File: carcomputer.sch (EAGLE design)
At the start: 39 parts, among them K1 351, Q1 BUZ10, Q2 BUZ10, T1 2N2219

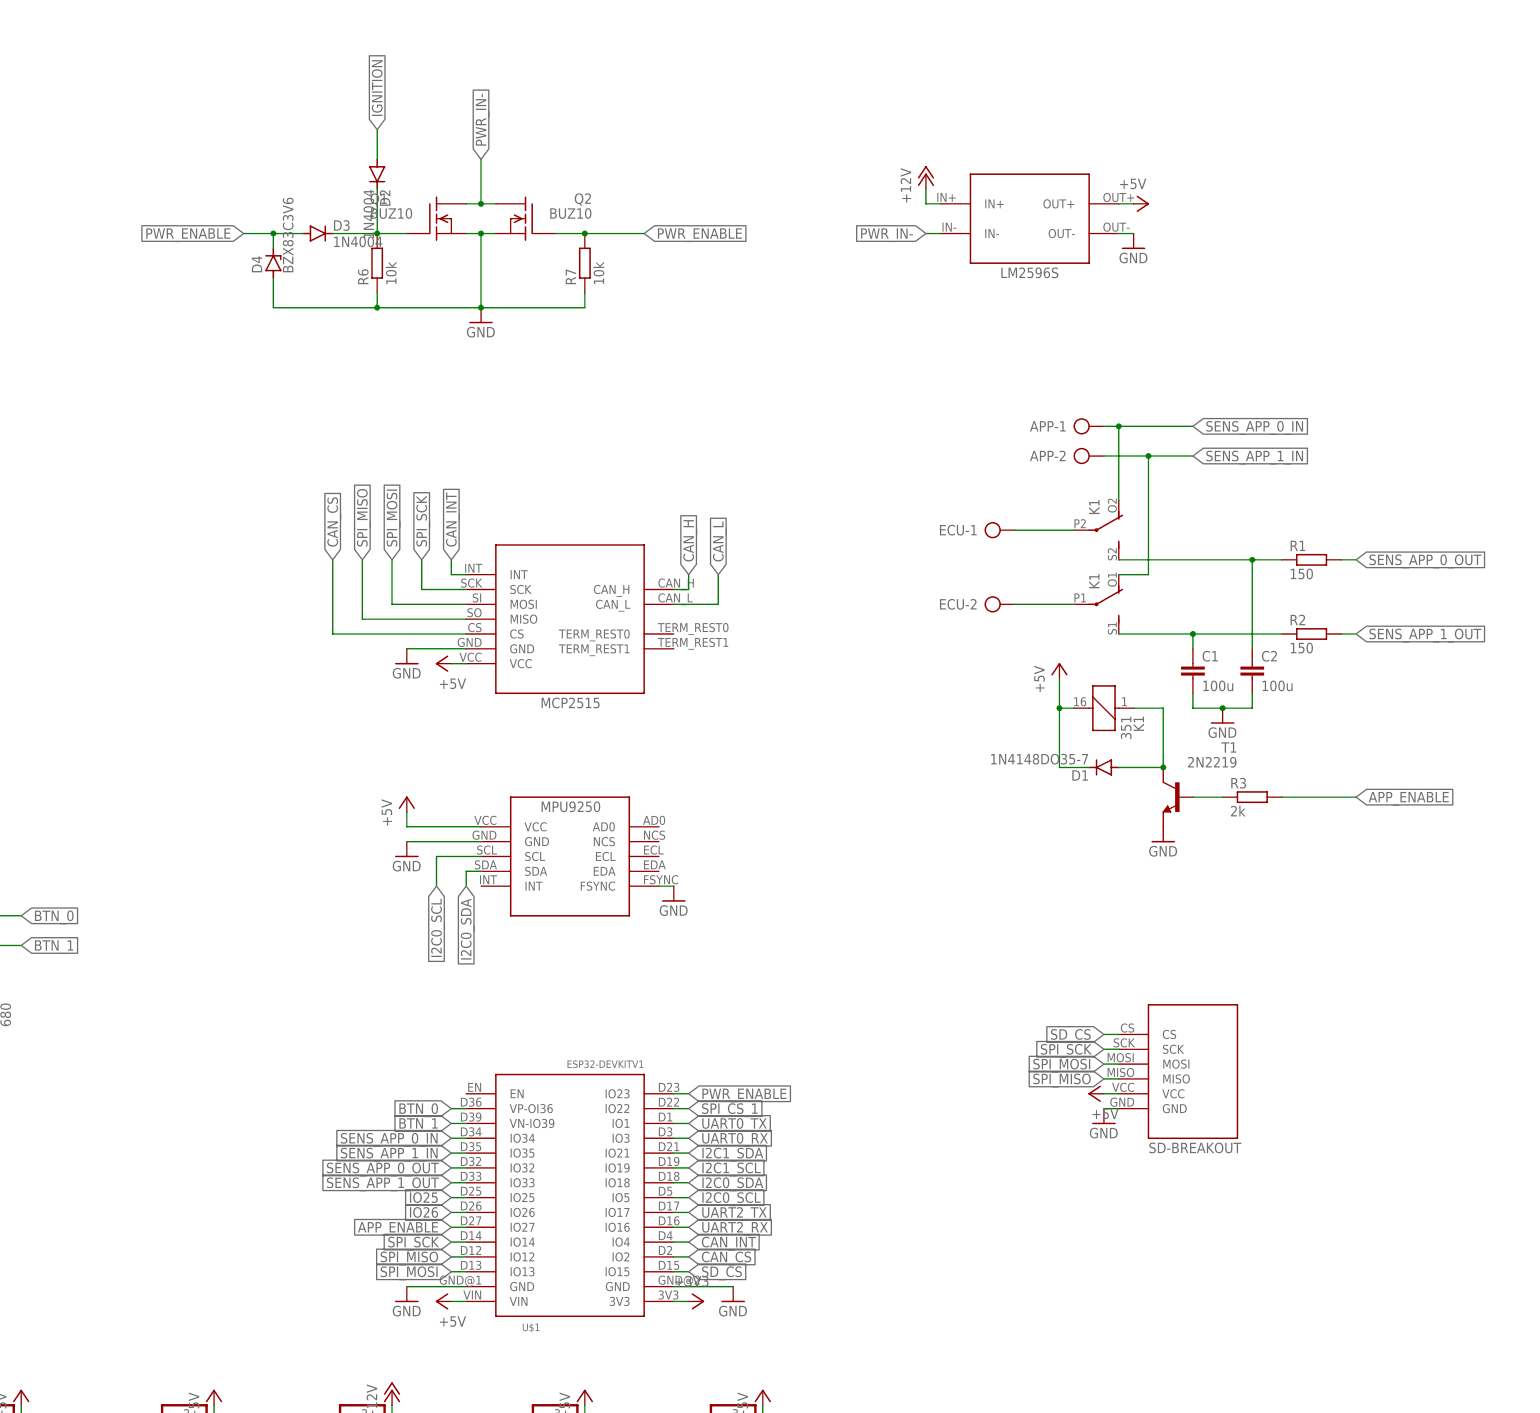
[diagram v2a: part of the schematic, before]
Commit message: Added voltage divider to input APP"
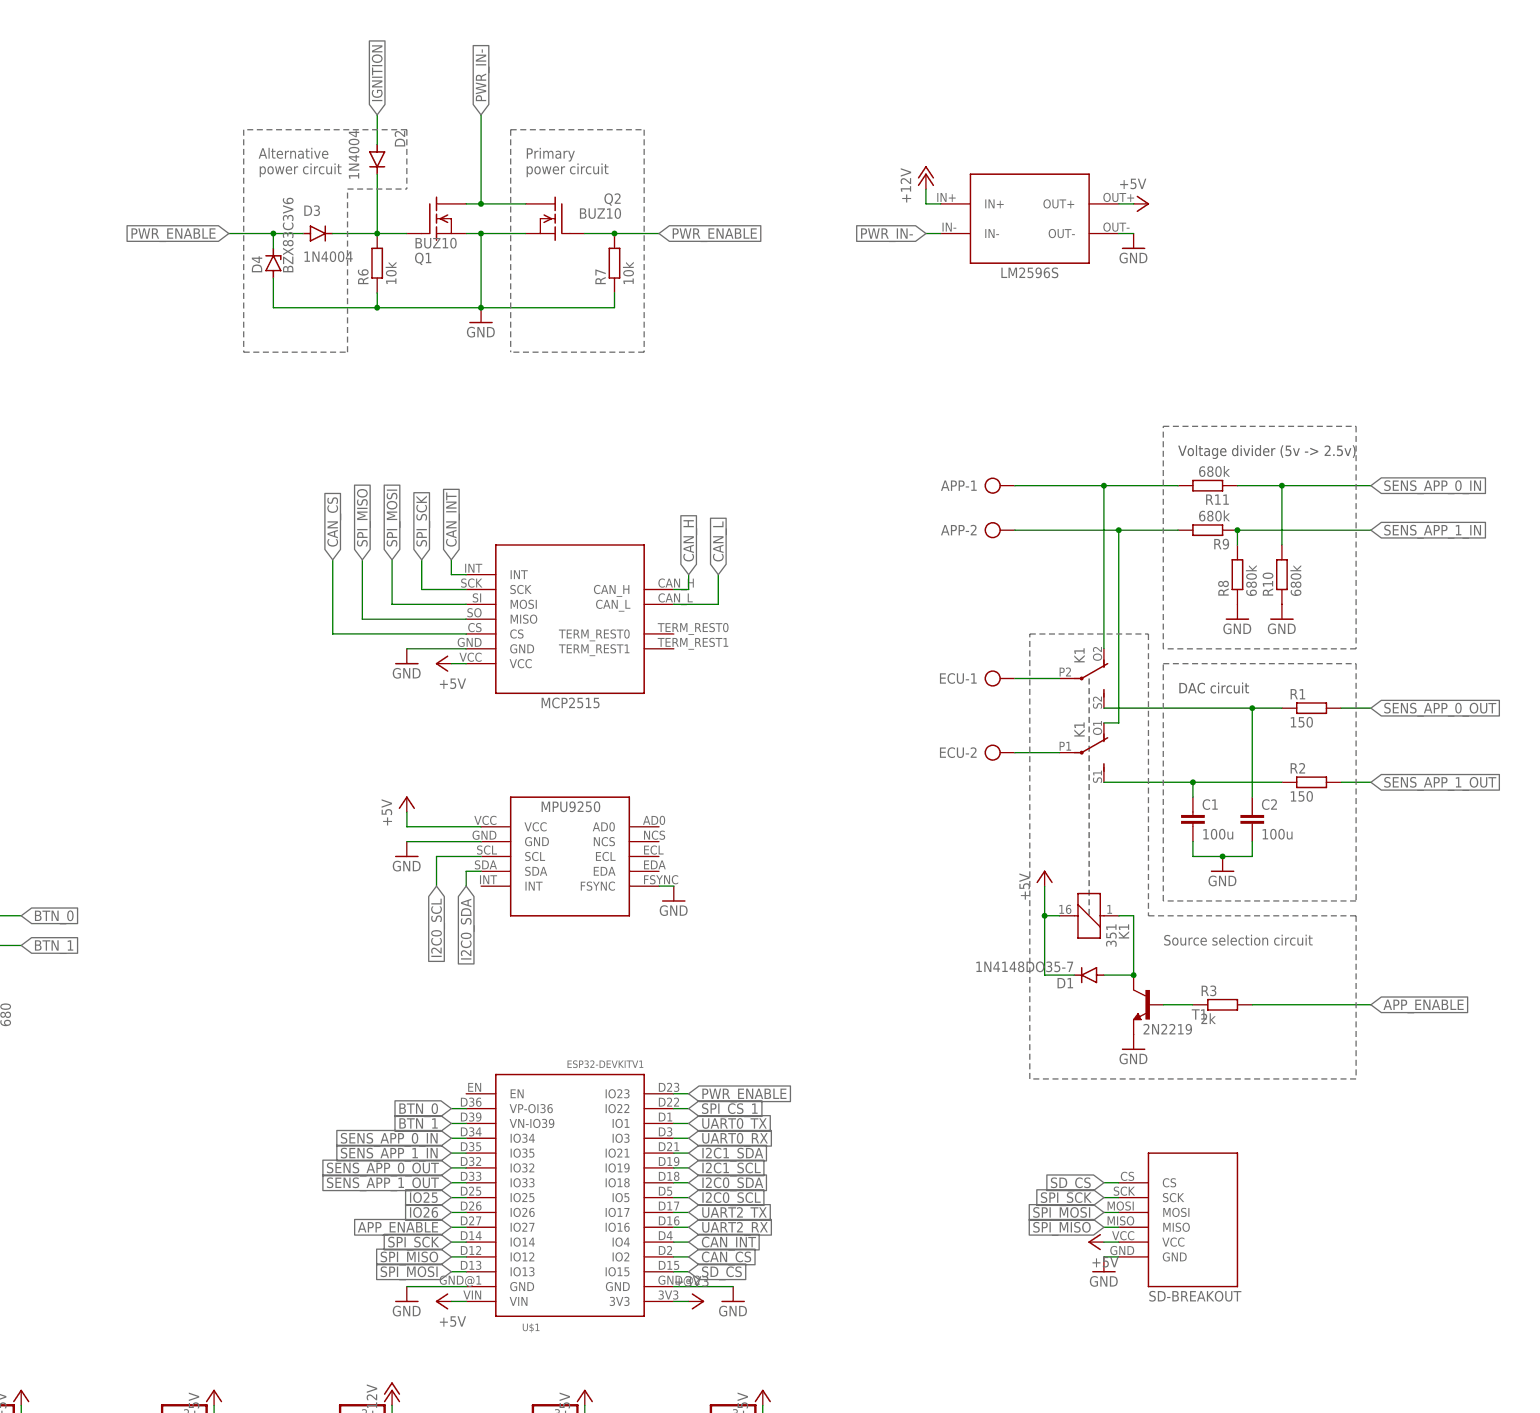
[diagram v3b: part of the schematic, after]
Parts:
- added R10, R11, R8, R9: 680k, rcl:R-EU_0207/7
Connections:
- new net APP_0_IN: APP-1.KL, K13.O, R11.2
- new net APP_1_IN: APP-2.KL, K12.O, R9.2
- net GND: now also R10.1, R8.1
- net SENS_APP_0_IN: now also R10.2, R11.1; no longer APP-1.KL, K13.O
- net SENS_APP_1_IN: now also R8.2, R9.1; no longer APP-2.KL, K12.O
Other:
- note added: "Alternative power circuit"
- note added: "DAC circuit"
- note added: "Primary power circuit"
- note added: "Source selection circuit"
- note added: "Voltage divider (5v -> 2.5v)"
- moved on the sheet: APP-1, APP-2, C1, C2, D1, D2, ECU-1, ECU-2, K1, Q2, R1, R2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

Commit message: Added A9G GPS unit. Removed backup files from git
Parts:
- added Q3, Q4: TIP136, transistor-pnp:TIP136
- added R12, R13, R14: 2k, rcl:R-EU_0207/7
- added R15: 5k, rcl:R-EU_0207/7
- added S1: (no value), switch-omron:10-XX
- added U$6: A9G, A9:A9G
- added U$7: BI-DIRECTIONAL1, level-converter:BI-DIRECTIONAL1
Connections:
- removed net SENS_APP_0_OUT: R1.2, U$1.IO32
- removed net SENS_APP_1_OUT: R2.2, U$1.IO33
- new net APP_PWM_OUT_0: R13.2, U$1.IO32
- new net APP_PWM_OUT_1: R12.2, U$1.IO33
- new net GPS_RX: U$6.IO0/RX1, U$7.RX_H1
- new net GPS_TX: U$6.IO1/TX1, U$7.TX_H1
- new net MCU_RESET: S1.P, S1.P1, U$1.EN, U$6.RST
- new net N$10: R14.1, U$2.INT
- new net N$11: Q4.C, R1.2
- new net N$13: Q4.B, R13.1
- new net N$8: Q3.B, R12.1
- new net N$9: Q3.C, R2.2
- net +3V3: now also DISPLAY-4.1, U$3.VCC, U$7.LV
- net +5V: now also Q3.E, Q4.E, U$6.5V, U$7.HV; no longer DISPLAY-4.1, U$3.VCC
- net CAN_INT: now also R14.2, R15.2; no longer U$2.INT
- net GND: now also R15.1, S1.S, S1.S1, U$6.GND, U$6.GND2, U$7.GND
- net SPI_MISO: now also U$1.IO13; no longer U$1.IO12
- net SPI_MOSI: now also U$1.IO12; no longer U$1.IO13
- net UART2_RX: now also U$7.RX_L1
- net UART2_TX: now also U$7.TX_L1
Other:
- moved on the sheet: APP-1, APP-2, C1, C2, D1, ECU-1, ECU-2, K1, R1, R10, R11, R2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

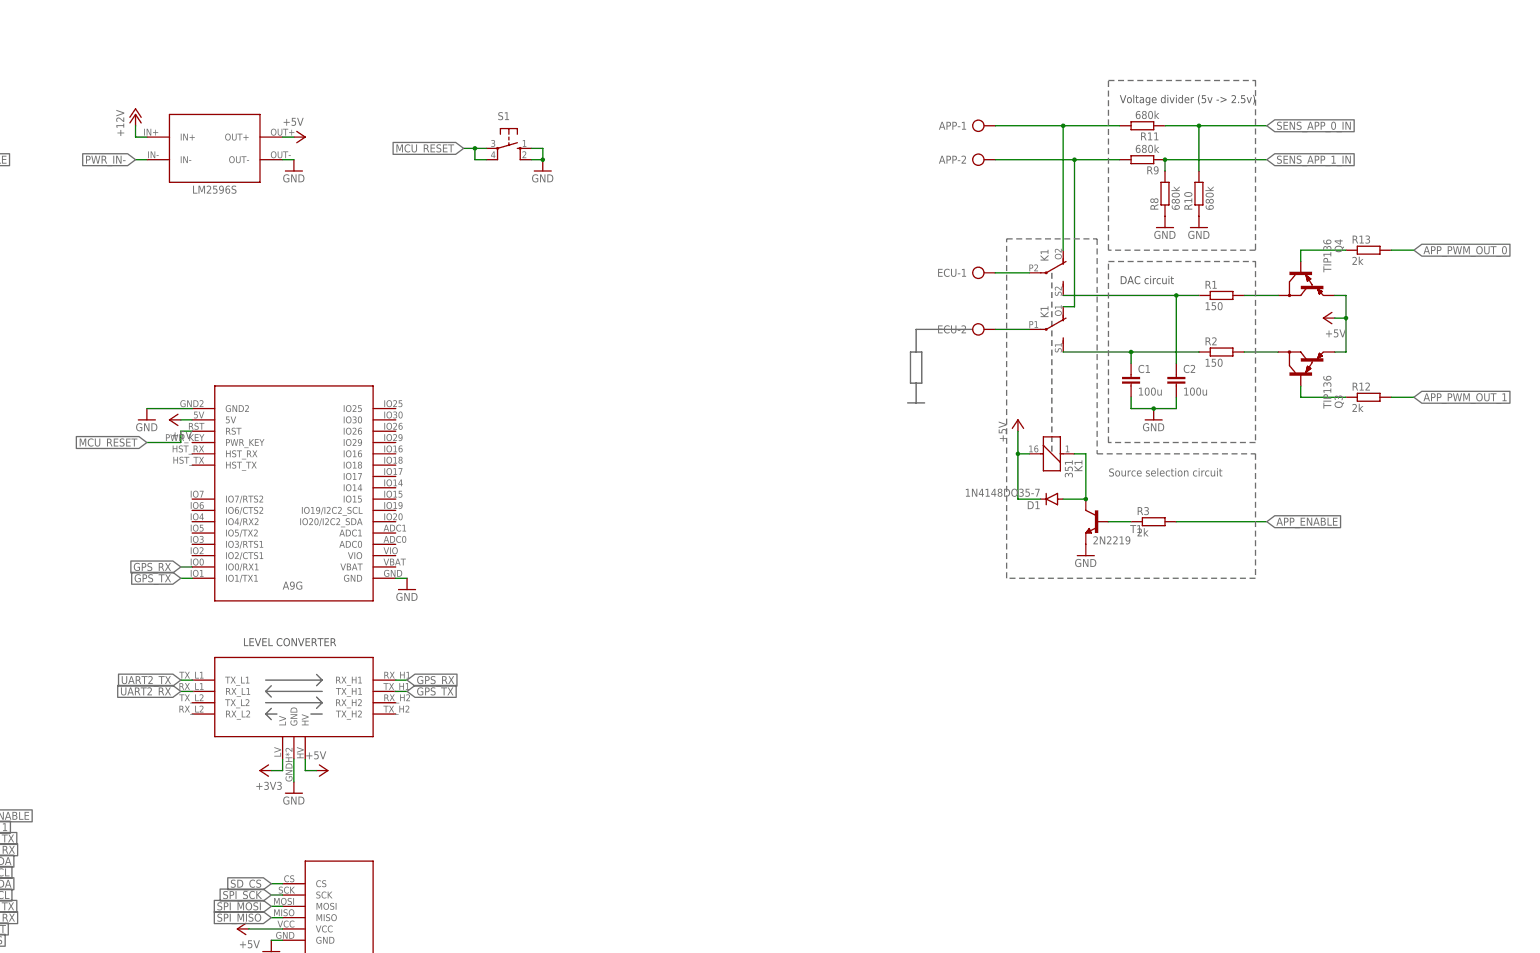
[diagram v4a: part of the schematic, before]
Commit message: Changed GPS level converter to external resistor using level converter internal resistor
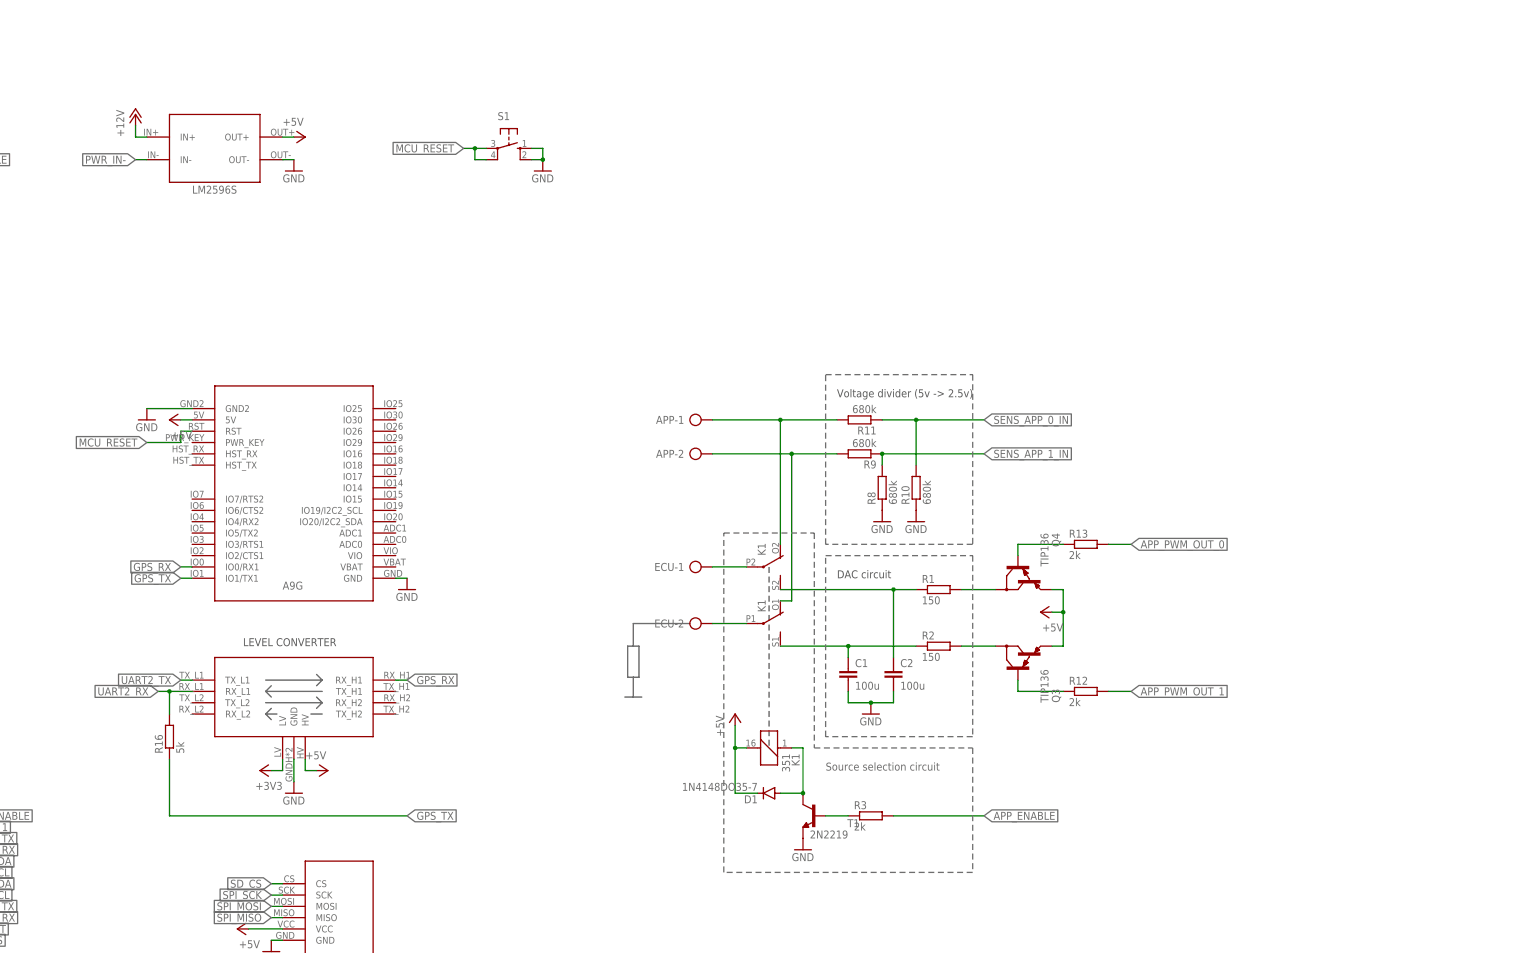
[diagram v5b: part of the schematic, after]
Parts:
- added R16: 5k, rcl:R-EU_0207/7
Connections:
- net GPS_TX: now also R16.1; no longer U$7.TX_H1
- net UART2_RX: now also R16.2
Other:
- moved on the sheet: APP-1, APP-2, C1, C2, D1, ECU-1, ECU-2, K1, Q3, Q4, R1, R10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

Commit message: Fixed power circuit
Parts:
- removed Q1, Q2: BUZ10, transistor-fet:BUZ10
- removed R7: 10k, rcl:R-EU_0207/7
- added Q5: TIP136, transistor-pnp:TIP136
- added R17: 26k, rcl:R-EU_0207/7
- added R18, R19: 10k, rcl:R-EU_0207/7
- added T2: 2N2219, transistor:2N2219
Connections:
- removed net PWR_IN-: Q1.D, Q2.D, U$4.IN-
- new net N$12: D2.A, R17.1
- new net N$14: Q5.B, R18.1
- new net N$15: R18.2, R19.1, T2.C
- new net PWR_IN+: Q5.C, U$4.IN+
- net +12V: now also Q5.E, R19.2; no longer U$4.IN+
- net GND: now also T2.E, U$4.IN-; no longer Q1.S, Q2.S, R7.1
- net IGNITION: now also R17.2; no longer D2.A
- net N$5: now also T2.B; no longer Q1.G
- net PWR_ENABLE: no longer Q2.G, R7.2
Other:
- note added: "?"
- note added: "ACCELERATOR PEDAL SWITCH/DAC"
- note added: "AUTO POWER MANAGEMENT"
- note added: "EXTRA CONNECTORS"
- note added: "Over voltage protection"
- note removed: "Alternative power circuit"
- note removed: "Primary power circuit"
- moved on the sheet: D2, D3, D4, JP_I2C_1, JP_I2C_2, JP_IO25, JP_IO26, JP_PWR_12V, JP_PWR_3V3, JP_PWR_5V_1, JP_PWR_5V_2, JP_SPI_1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

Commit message: Fixed 3V->5V gas pedal converter at high frequencies with opamp after DAC
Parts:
- removed Q3, Q4: TIP136, transistor-pnp:TIP136
- added C3: 100u, rcl:C-EU025-050X050
- added D5, D6: BZX83C5V6, diode:BZX85
- added D7, D8: 1N4148DO35-7, diode:1N4148DO35-7
- added IC1: LM358N, linear:LM358N
- added Q6: BUZ72, transistor-fet:BUZ72
- added Q7: BUZ171, transistor-fet:BUZ171
- added R20, R28, R7: 2k, rcl:R-EU_0207/7
- added R21, R26: 1k, rcl:R-EU_0207/7
- added R24: 150, rcl:R-EU_0207/7
- added R25: 500?, rcl:R-EU_0207/7
- added R27: 10k, rcl:R-EU_0207/7
- R12, R13: value 2k -> 1k
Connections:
- new net IN: Q6.G, R28.2
- new net N$16: IC1B.-IN, R13.2, R20.1
- new net N$21: C3.1, R24.2, R25.2
- new net N$24: Q7.G, R26.2, R27.1
- new net OUT: Q7.D, R24.1
- net +12V: now also IC1P.V+
- net +5V: now also D7.C, D8.C, Q7.S, R27.2; no longer Q3.E, Q4.E
- net APP_PWM_OUT_0: now also R1.2; no longer R13.2
- net APP_PWM_OUT_1: now also R2.2; no longer R12.2
- net GND: now also C3.2, D5.A, D6.A, IC1P.V-, Q6.D, Q6.S, R20.2, R25.1, R26.1, R28.1, R7.2
- net GPS_RX: now also JP_UART2.2
- net GPS_TX: now also JP_UART2.3
- net N$11: now also D3.A, D4.C, R21.1; no longer Q4.C, R1.2
- net N$13: now also IC1A.-IN, R12.2, R7.1; no longer Q4.B, R13.1
- net N$14: now also R19.1
- net N$15: no longer R19.1
- net N$3: now also D6.C, D8.A, IC1B.OUT, R13.1; no longer C1.1, R2.1
- net N$4: now also D5.C, D7.A, IC1A.OUT, R12.1; no longer C2.1, R1.1
- net N$8: now also C2.1, IC1A.+IN, R1.1; no longer Q3.B, R12.1
- net N$9: now also C1.1, IC1B.+IN, R2.1; no longer Q3.C, R2.2
- net PWR_ENABLE: now also R21.2; no longer D3.A, D4.C
- net UART2_RX: no longer JP_UART2.2
- net UART2_TX: no longer JP_UART2.3
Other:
- note added: "- +14V"
- note added: "3.3V PWM 80 kHz"
- note added: "5V PWM"
- note added: "???"
- note added: "Checked"
- note added: "DAC"
- note added: "Gain 3.3V -> 5V"
- note added: "Load"
- note removed: "?"
- moved on the sheet: APP-1, APP-2, C1, C2, ECU-1, K1, Q5, R1, R10, R11, R12, R13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

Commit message: Fixed overvoltage protection on gas pedal circuit
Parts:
- removed D7, D8: 1N4148DO35-7, diode:1N4148DO35-7
- removed U$7: BI-DIRECTIONAL1, level-converter:BI-DIRECTIONAL1
- added C4: 0.1u, rcl:C-EU025-050X050
- added Q1: BS170, transistor-small-signal:BS170
- added R22, R23, R29: 10k, rcl:R-EU_0207/7
- added R30, R31: >65, rcl:R-EU_0207/7
- D5, D6: value BZX83C5V6 -> BZX83C5V1
- R10, R11, R8, R9: value 680k -> 10k
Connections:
- new net N$17: D5.C, K13.S, R30.1
- new net N$18: IC1B.OUT, R13.1, R31.2
- net +12V: now also C4.1
- net +3V3: now also Q1.G, R22.2; no longer U$7.LV
- net +5V: now also R23.2; no longer D7.C, D8.C, U$7.HV
- net GND: now also C4.2, R29.1; no longer U$7.GND
- net GPS_RX: now also Q1.D, R23.1; no longer U$7.RX_H1
- net N$3: now also R31.1; no longer D8.A, IC1B.OUT, R13.1
- net N$4: now also R30.2; no longer D5.C, D7.A, K13.S
- net UART2_RX: now also R29.2; no longer U$7.RX_L1
- net UART2_TX: now also Q1.S, R22.1; no longer U$7.TX_L1
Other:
- note added: "EXAMPLES"
- note added: "LEVEL CONVERTER"
- moved on the sheet: C1, C2, D5, D6, IC1A, IC1B, R1, R12, R13, R16, R2, R20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
